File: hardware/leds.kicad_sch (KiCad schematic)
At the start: 17 parts

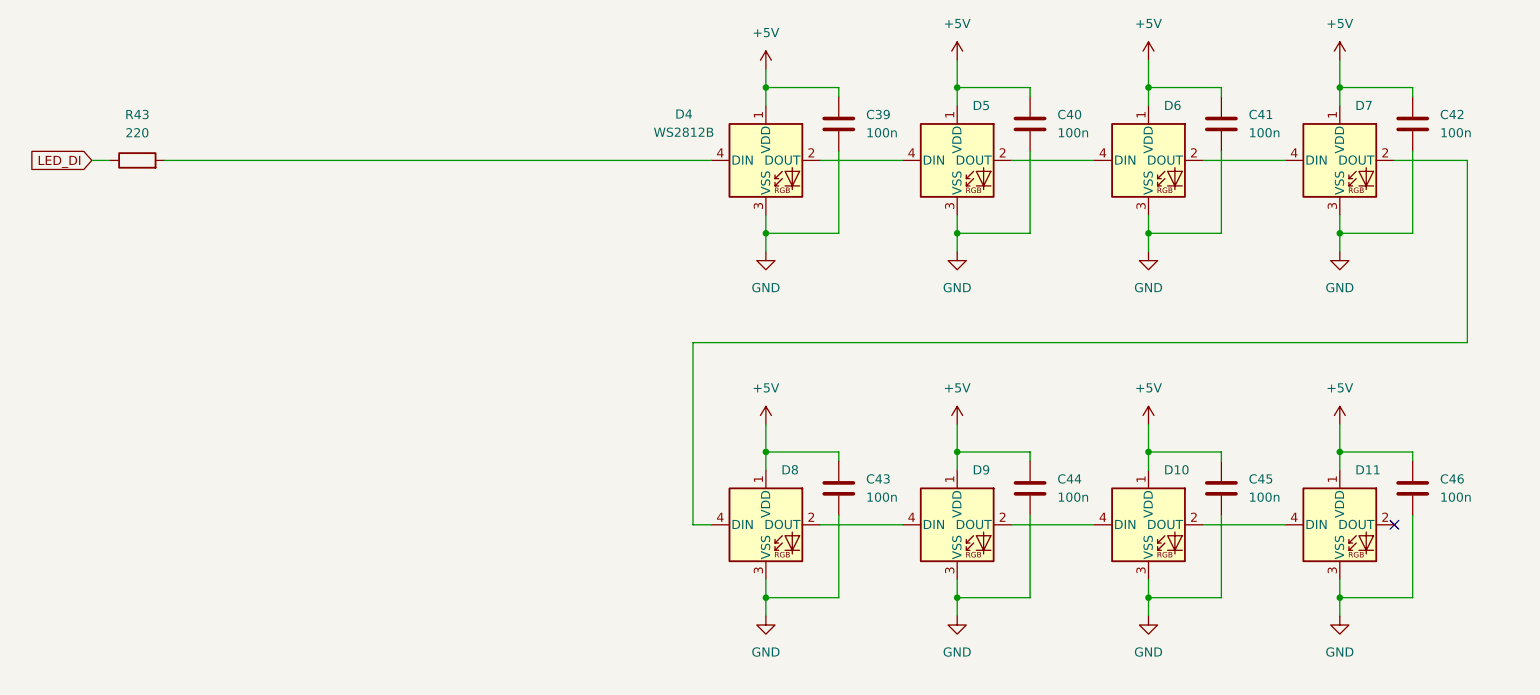
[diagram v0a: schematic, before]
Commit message: added basic PCB ordering
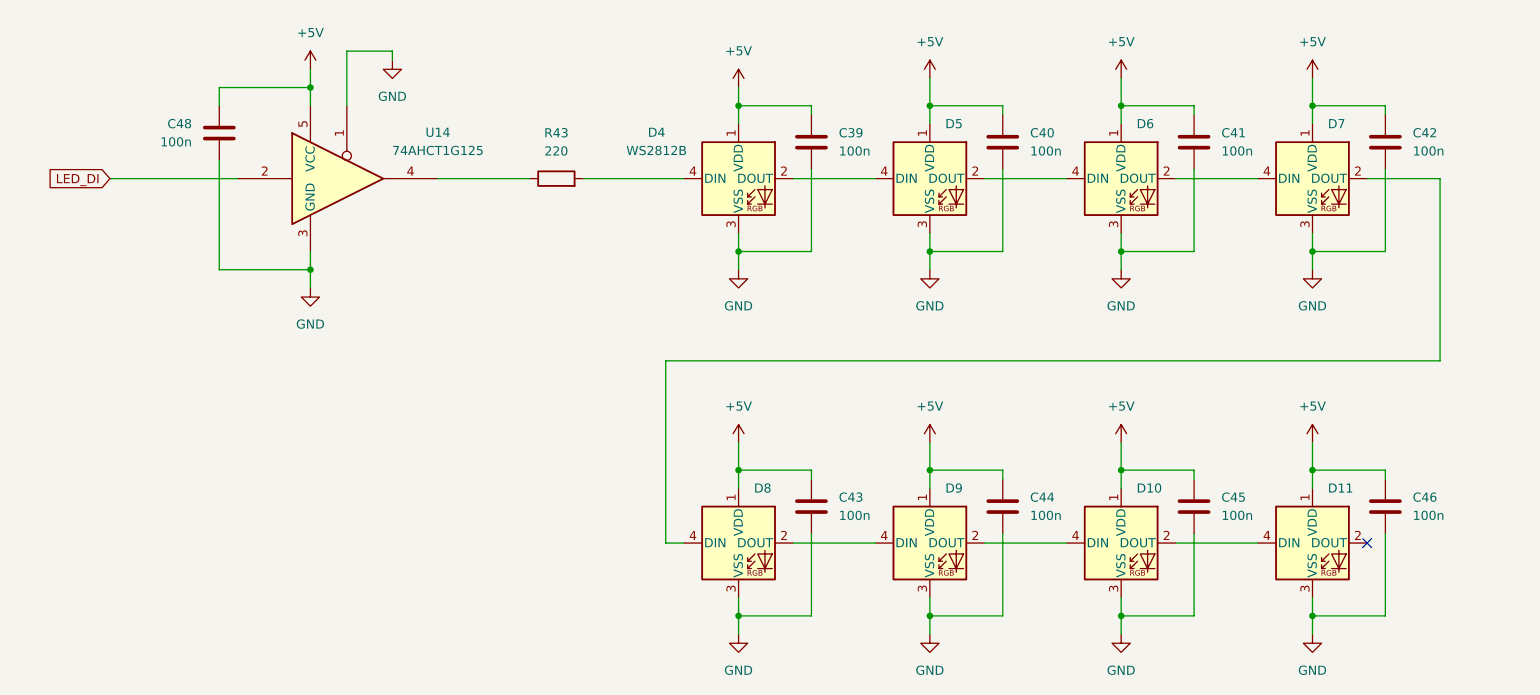
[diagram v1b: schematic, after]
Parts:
- added C48: 100n, Capacitor_SMD:C_0603_1608Metric, symbol Device:C
- added U14: 74AHCT1G125, Package_TO_SOT_SMD:SOT-353_SC-70-5, symbol 74xGxx:74AHCT1G125
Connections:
- net +5V: now also C48.1, U14.5 (VCC)
- net GND: now also C48.2, U14.1, U14.3 (GND)
- net LED_DI: now also U14.2; no longer R43.1
- new net: R43.1, U14.4
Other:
- moved on the sheet: C39, C40, C41, C42, C43, C44, C45, C46, D10, D11, D4, D5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

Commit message: added all footprints, updated to 0805, added layout for Jacks
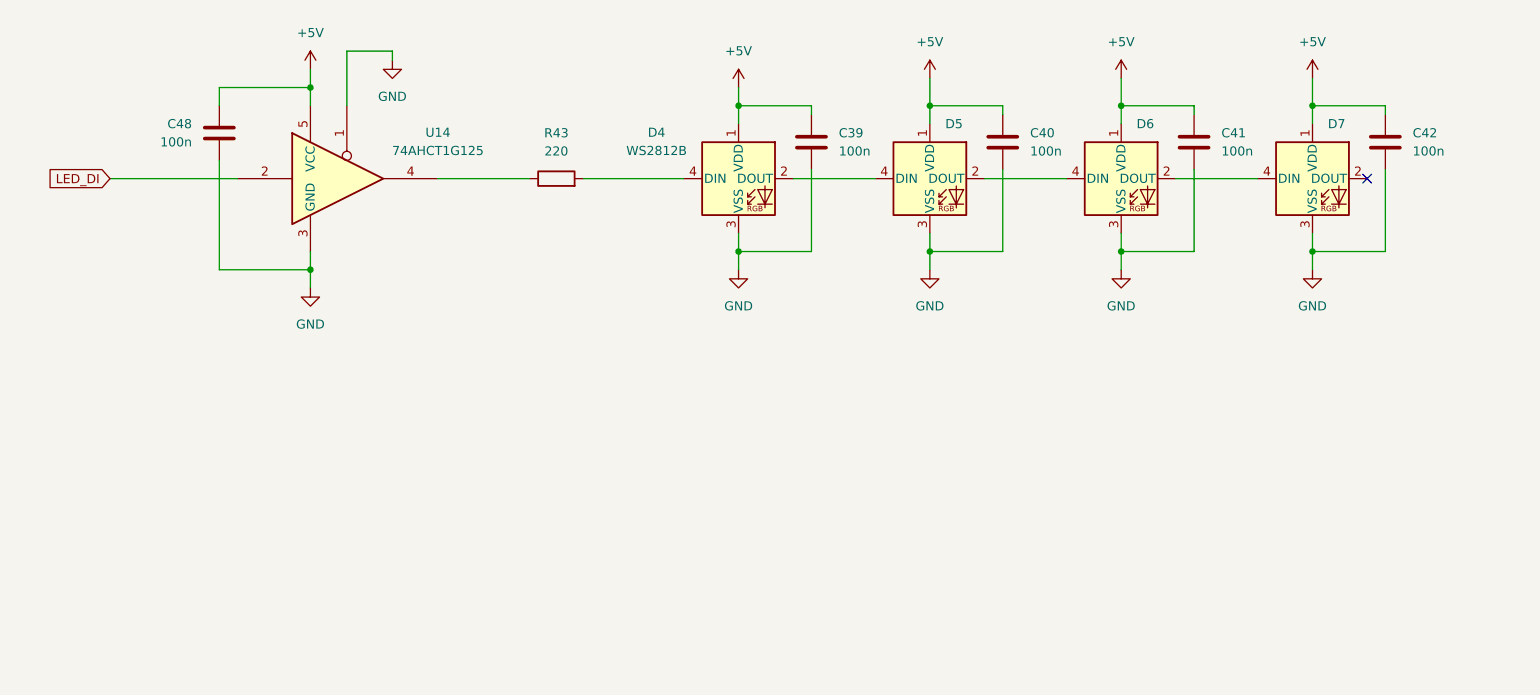
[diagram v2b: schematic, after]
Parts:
- removed C43, C44, C45, C46: 100n, Capacitor_SMD:C_0603_1608Metric, symbol Device:C
- removed D10, D11, D8, D9: WS2812B, LED_SMD:LED_WS2812B_PLCC4_5.0x5.0mm_P3.2mm, symbol LED:WS2812B
- C39, C40, C41, C42, C48: footprint Capacitor_SMD:C_0603_1608Metric -> Capacitor_SMD:C_0805_2012Metric
- R43: footprint Resistor_SMD:R_0603_1608Metric -> Resistor_SMD:R_0805_2012Metric

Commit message: replaced buffer ICs with analog switches, schematic bugfixes, started new routing
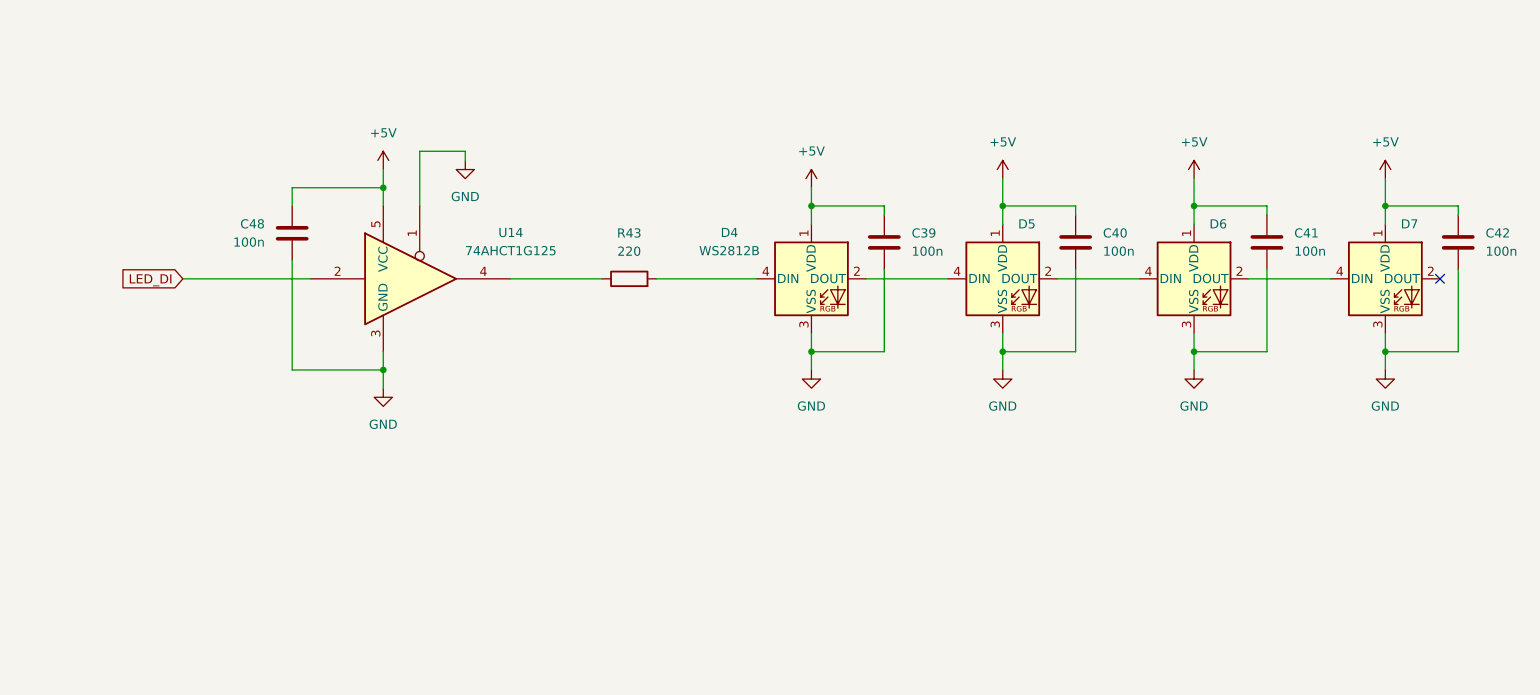
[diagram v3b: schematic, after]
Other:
- moved on the sheet: C39, C40, C41, C42, C48, D4, D5, D6, D7, R43, U14

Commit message: added mouser part numbers
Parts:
- C39, C40, C41, C42, C48, R43: Part Source (none) -> Uni
- D4, D5, D6, D7: Mouser No (none) -> 485-1655; Part Source (none) -> Mouser
- U14: Mouser No (none) -> 595-74AHCT1G125DCKRG; Part Source (none) -> Mouser

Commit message: added signed declaration and updated schematic names
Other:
- company: (none) -> Amon Benson, TU Berlin
- title: (none) -> LEDs
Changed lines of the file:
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@@
 	(generator_version "10.0")
 	(paper "A4")
+	(title_block
+		(title "LEDs")
+		(date "2026-09-27")
+		(rev "1.0")
+		(company "Amon Benson, TU Berlin")
+	)
 	(junction
 		(at 82.55 104.14)
